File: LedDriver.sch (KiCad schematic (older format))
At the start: 0 parts

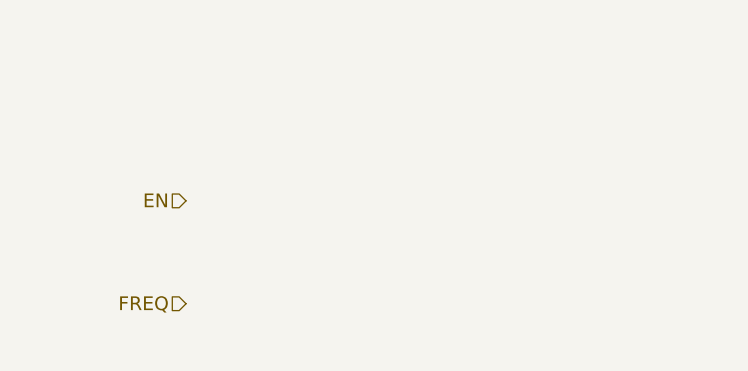
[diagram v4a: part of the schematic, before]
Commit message: Added LED Driver
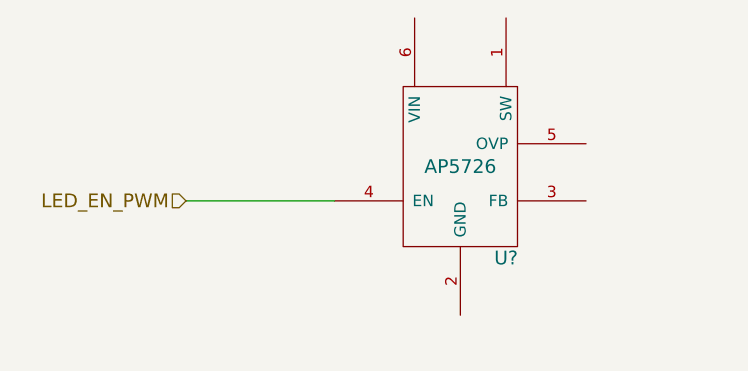
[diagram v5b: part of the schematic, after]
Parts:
- added U?: AP5726, symbol AP5726
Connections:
- new net LED_EN_PWM: U?.4 (EN)
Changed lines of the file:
@@
 $Descr A4 11693 8268
 encoding utf-8
-Sheet 6 9
+Sheet 5 9
 Title ""
-Date "4 oct 2013"
+Date "11 oct 2013"
 Rev ""
 Comp ""
@@
 $EndDescr
 Text HLabel 1400 1700 0    60   Input ~ 0
-EN
-Text HLabel 1400 2150 0    60   Input ~ 0
-FREQ
+LED_EN_PWM
 Text HLabel 8850 1850 0    60   Output ~ 0
 STRING+
 Text HLabel 8850 2300 0    60   Input ~ 0
 STRING-
+$Comp
+L AP5726 U?
+U 1 1 52575F25
+P 2600 1500
+F 0 "U?" H 2800 1050 60  0000 C CNN
+F 1 "AP5726" H 2600 1450 60  0000 C CNN
+F 2 "" H 2550 1000 60  0000 C CNN
+F 3 "" H 2550 1000 60  0000 C CNN
+	1    2600 1500
+	1    0    0    -1
+$EndComp
+Wire Wire Line
+	1400 1700 2050 1700
 $EndSCHEMATC

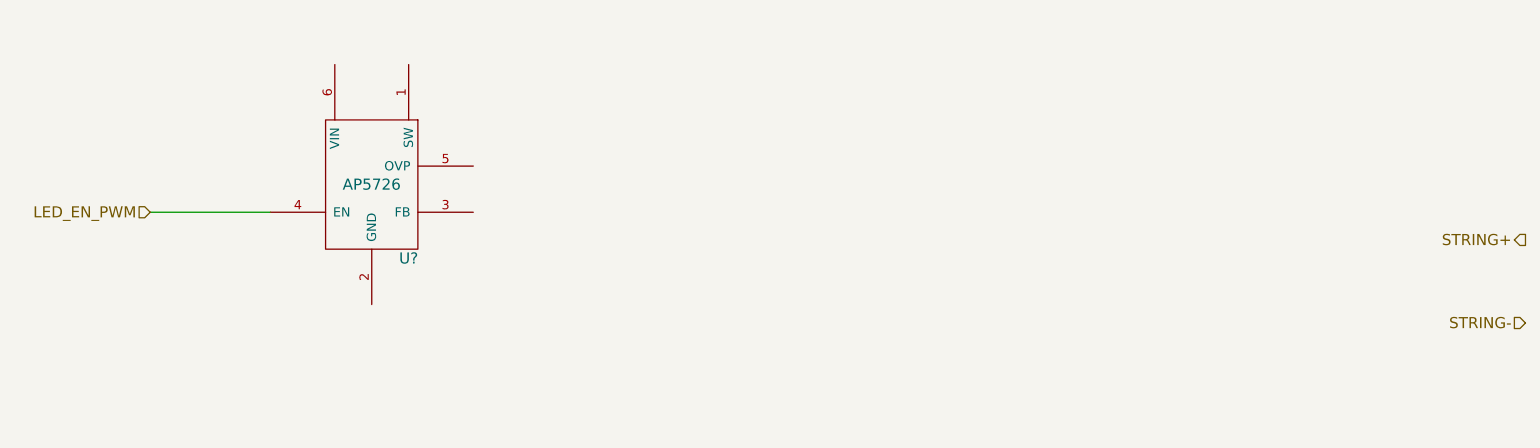
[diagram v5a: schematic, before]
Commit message: Added connections to Terminal Block
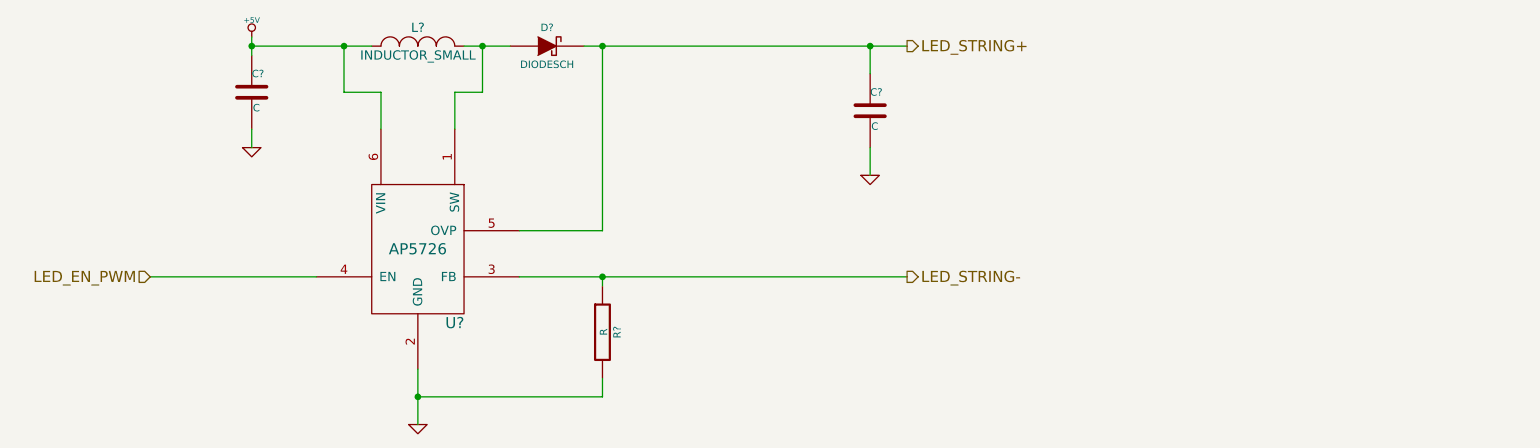
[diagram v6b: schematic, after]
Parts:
- removed U?: AP5726, symbol AP5726
- added C? (x2): C, ~, symbol C
- added D?: DIODESCH, ~, symbol DIODESCH
- added L?: INDUCTOR_SMALL, ~, symbol INDUCTOR_SMALL
- added R?: R, ~, symbol R
- added U?: AP5726, symbol AP5726
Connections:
- net LED_EN_PWM: now also U?.4 (EN)
- new net: D?.1 (A), L?.2, U?.1 (SW)
- new net +5V: C?.1, L?.1, U?.6 (VIN)
- new net GND: C?.2, C?.2, R?.2, U?.2 (GND)
- new net LED_STRING+: C?.1, D?.2 (K), U?.5 (OVP)
- new net LED_STRING-: R?.1, U?.3 (FB)
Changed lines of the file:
@@
 $Descr A4 11693 8268
 encoding utf-8
-Sheet 5 9
+Sheet 9 9
 Title ""
 Date "11 oct 2013"
@@
 Comment4 ""
 $EndDescr
-Text HLabel 1400 1700 0    60   Input ~ 0
+Text HLabel 1400 2050 0    60   Input ~ 0
 LED_EN_PWM
-Text HLabel 8850 1850 0    60   Output ~ 0
-STRING+
-Text HLabel 8850 2300 0    60   Input ~ 0
-STRING-
+Text HLabel 5500 800  2    60   Output ~ 0
+LED_STRING+
+Text HLabel 5500 2050 2    60   Output ~ 0
+LED_STRING-
 $Comp
-L AP5726 U?
-U 1 1 52575F25
-P 2600 1500
-F 0 "U?" H 2800 1050 60  0000 C CNN
-F 1 "AP5726" H 2600 1450 60  0000 C CNN
-F 2 "" H 2550 1000 60  0000 C CNN
-F 3 "" H 2550 1000 60  0000 C CNN
-	1    2600 1500
+L +5V #PWR?
+U 1 1 52576BAC
+P 1950 750
+F 0 "#PWR?" H 1950 840 20  0001 C CNN
+F 1 "+5V" H 1950 840 30  0000 C CNN
+F 2 "~" H 1950 750 60  0000 C CNN
+F 3 "~" H 1950 750 60  0000 C CNN
+	1    1950 750
+	1    0    0    -1
+$EndComp
+$Comp
+L GND #PWR?
+U 1 1 52576BC5
+P 1950 1350
+F 0 "#PWR?" H 1950 1350 30  0001 C CNN
+F 1 "GND" H 1950 1280 30  0001 C CNN
+F 2 "~" H 1950 1350 60  0000 C CNN
+F 3 "~" H 1950 1350 60  0000 C CNN
+	1    1950 1350
+	1    0    0    -1
+$EndComp
+$Comp
+L C C?
+U 1 1 52576BD4
+P 1950 1050
+F 0 "C?" H 1950 1150 40  0000 L CNN
+F 1 "C" H 1956 965 40  0000 L CNN
+F 2 "~" H 1988 900 30  0000 C CNN
+F 3 "~" H 1950 1050 60  0000 C CNN
+	1    1950 1050
 	1    0    0    -1
 $EndComp
 Wire Wire Line
-	1400 1700 2050 1700
+	1950 750  1950 850
+Wire Wire Line
+	1950 1250 1950 1350
+Connection ~ 1950 800
+Wire Wire Line
+	1400 2050 2300 2050
+$Comp
+L INDUCTOR_SMALL L?
+U 1 1 52576C3D
+P 2850 800
+F 0 "L?" H 2850 900 50  0000 C CNN
+F 1 "INDUCTOR_SMALL" H 2850 750 50  0000 C CNN
+F 2 "~" H 2850 800 60  0000 C CNN
+F 3 "~" H 2850 800 60  0000 C CNN
+	1    2850 800
+	1    0    0    -1
+$EndComp
+Wire Wire Line
+	1950 800  2600 800
+Wire Wire Line
+	2450 800  2450 1050
+Wire Wire Line
+	2450 1050 2650 1050
+Connection ~ 2450 800
+Wire Wire Line
+	3100 800  3350 800
+Wire Wire Line
+	3200 800  3200 1050
+Wire Wire Line
+	3200 1050 3050 1050
+Connection ~ 3200 800
+$Comp
+L C C?
+U 1 1 52576C8D
+P 5300 1150
+F 0 "C?" H 5300 1250 40  0000 L CNN
+F 1 "C" H 5306 1065 40  0000 L CNN
+F 2 "~" H 5338 1000 30  0000 C CNN
+F 3 "~" H 5300 1150 60  0000 C CNN
+	1    5300 1150
+	1    0    0    -1
+$EndComp
+$Comp
+L GND #PWR?
+U 1 1 52576CA4
+P 5300 1500
+F 0 "#PWR?" H 5300 1500 30  0001 C CNN
+F 1 "GND" H 5300 1430 30  0001 C CNN
+F 2 "~" H 5300 1500 60  0000 C CNN
+F 3 "~" H 5300 1500 60  0000 C CNN
+	1    5300 1500
+	1    0    0    -1
+$EndComp
+$Comp
+L DIODESCH D?
+U 1 1 52576CBB
+P 3550 800
+F 0 "D?" H 3550 900 40  0000 C CNN
+F 1 "DIODESCH" H 3550 700 40  0000 C CNN
+F 2 "~" H 3550 800 60  0000 C CNN
+F 3 "~" H 3550 800 60  0000 C CNN
+	1    3550 800
+	1    0    0    -1
+$EndComp
+$Comp
+L AP5726 U?
+U 1 1 52576DA6
+P 2850 1850
+F 0 "U?" H 3050 1400 60  0000 C CNN
+F 1 "AP5726" H 2850 1800 60  0000 C CNN
+F 2 "" H 2800 1350 60  0000 C CNN
+F 3 "" H 2800 1350 60  0000 C CNN
+	1    2850 1850
+	1    0    0    -1
+$EndComp
+Wire Wire Line
+	2650 1050 2650 1250
+Wire Wire Line
+	3050 1050 3050 1250
+Wire Wire Line
+	3750 800  5500 800
+Wire Wire Line
+	3850 800  3850 1800
+Wire Wire Line
+	3850 1800 3400 1800
+Connection ~ 3850 800
+$Comp
+L R R?
+U 1 1 52576E18
+P 3850 2350
+F 0 "R?" V 3930 2350 40  0000 C CNN
+F 1 "R" V 3857 2351 40  0000 C CNN
+F 2 "~" V 3780 2350 30  0000 C CNN
+F 3 "~" H 3850 2350 30  0000 C CNN
+	1    3850 2350
+	1    0    0    -1
+$EndComp
+Wire Wire Line
+	3400 2050 5500 2050
+Wire Wire Line
+	3850 2100 3850 2050
+Connection ~ 3850 2050
+$Comp
+L GND #PWR?
+U 1 1 52576E57
+P 2850 2850
+F 0 "#PWR?" H 2850 2850 30  0001 C CNN
+F 1 "GND" H 2850 2780 30  0001 C CNN
+F 2 "~" H 2850 2850 60  0000 C CNN
+F 3 "~" H 2850 2850 60  0000 C CNN
+	1    2850 2850
+	1    0    0    -1
+$EndComp
+Wire Wire Line
+	2850 2550 2850 2850
+Wire Wire Line
+	3850 2600 3850 2700
+Wire Wire Line
+	3850 2700 2850 2700
+Connection ~ 2850 2700
+Wire Wire Line
+	5300 950  5300 800
+Connection ~ 5300 800
+Wire Wire Line
+	5300 1350 5300 1500
 $EndSCHEMATC
